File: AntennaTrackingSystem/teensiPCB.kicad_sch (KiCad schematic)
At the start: 0 parts

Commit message: 1st schematic built and added footprints
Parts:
- added C1: 0.1uF, Capacitor_SMD:C_0603_1608Metric, symbol Device:C
- added C2: 1uF, Capacitor_SMD:C_0603_1608Metric, symbol Device:C
- added J1: UART1, Connector_PinHeader_2.54mm:PinHeader_1x04_P2.54mm_Vertical, symbol Connector:Conn_01x04_Pin
- added J2: UART2, Connector_PinHeader_2.54mm:PinHeader_1x04_P2.54mm_Vertical, symbol Connector:Conn_01x04_Pin
- added J3: I2C ext, Connector_PinHeader_2.54mm:PinHeader_1x04_P2.54mm_Vertical, symbol Connector:Conn_01x04_Pin
- added J4: screw terminal, TerminalBlock_MetzConnect:TerminalBlock_MetzConnect_Type073_RT02602HBLU_1x02_P5.08mm_Horizontal, symbol Connector:Screw_Terminal_01x02
- added R1, R2: 4.7k, Resistor_SMD:R_0603_1608Metric, symbol Device:R
- added U1: Teensy4.1, Teensy41:Teensy41, symbol teensy:Teensy4.1
- added U2: SAM-M10Q-00B, SAM M10Q footprint:SAM-M10Q_UBL, symbol 2026-03-27_00-02-23:SAM-M10Q-00B
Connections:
- new net: J2.RX (Pin_2), U1.10 (8_TX2_IN1)
- new net: J2.TX (Pin_1), U1.9 (7_RX2_OUT1A)
- new net: J3.SCL (Pin_1), U1.16 (24_A10_TX6_SCL2)
- new net: J3.SDA (Pin_2), U1.17 (25_A11_RX6_SDA2)
- new net: J1.TX (Pin_1), U1.2 (0_RX1_CRX2_CS1)
- new net: J1.RX (Pin_2), U1.3 (1_TX1_CTX2_MISO1)
- new net: R2.1, U1.38 (16_A2_RX4_SCL1), U2.12 (SCL)
- new net: R1.2, U1.39 (17_A3_TX4_SDA1), U2.9 (SDA)
- new net: J4.2 (Pin_2), U1.48 (VIN)
- new net +3.3V: C1.1, C2.1, J1.3V3 (Pin_3), J2.3V3 (Pin_3), J3.3V3 (Pin_3), R1.1, R2.2, U1.15 (3V3), U1.46 (3V3), U2.17 (VCC)
- new net GND: C1.2, C2.2, J1.GND (Pin_4), J2.GND (Pin_4), J3.GND (Pin_4), J4.1 (Pin_1), U1.1 (GND), U1.47 (GND), U2.1 (GND), U2.10 (GND), U2.11 (GND), U2.15 (GND), U2.16 (GND), U2.20 (GND), U2.4 (GND), U2.5 (GND), U2.6 (GND)
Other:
- note added: "decoupling capacitors"
- note added: "pull up resistors"

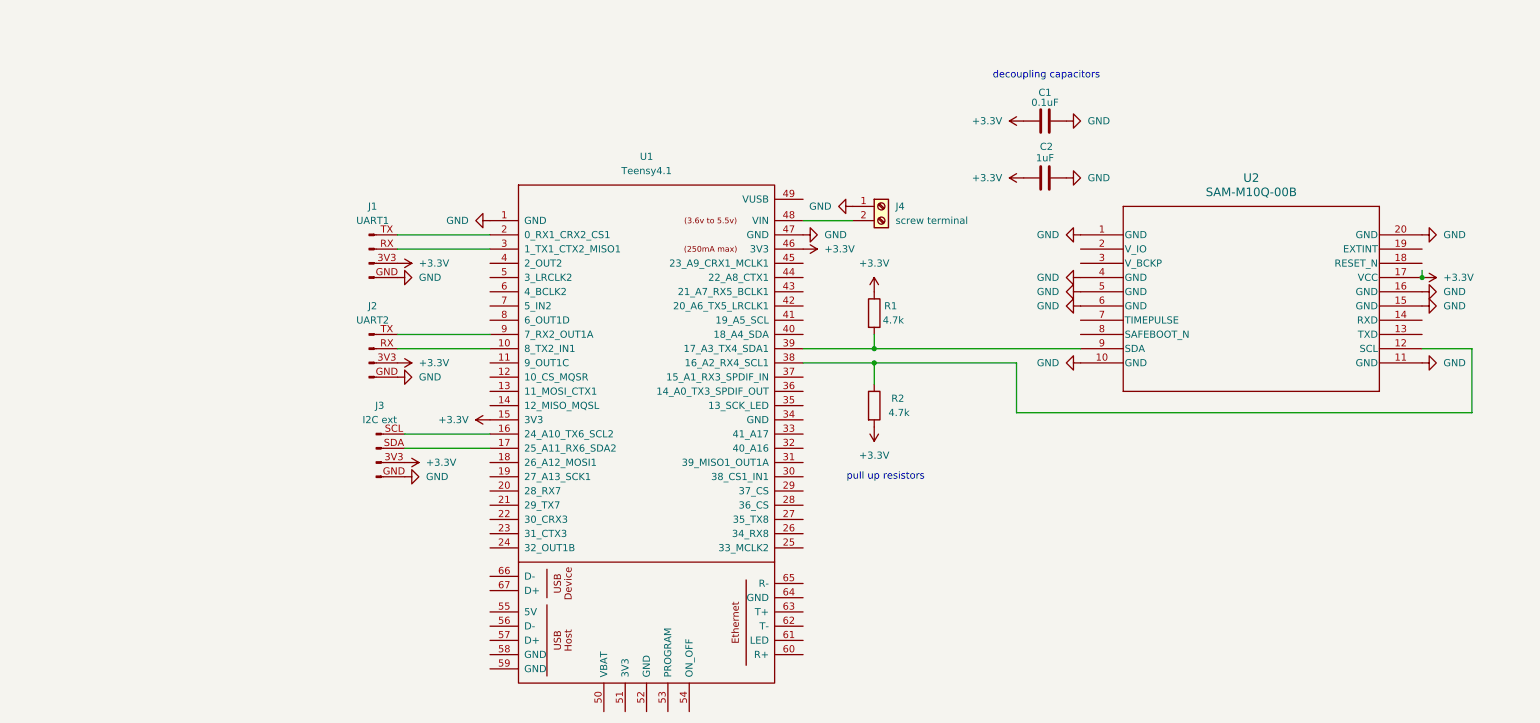
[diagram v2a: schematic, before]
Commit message: schematic review changes
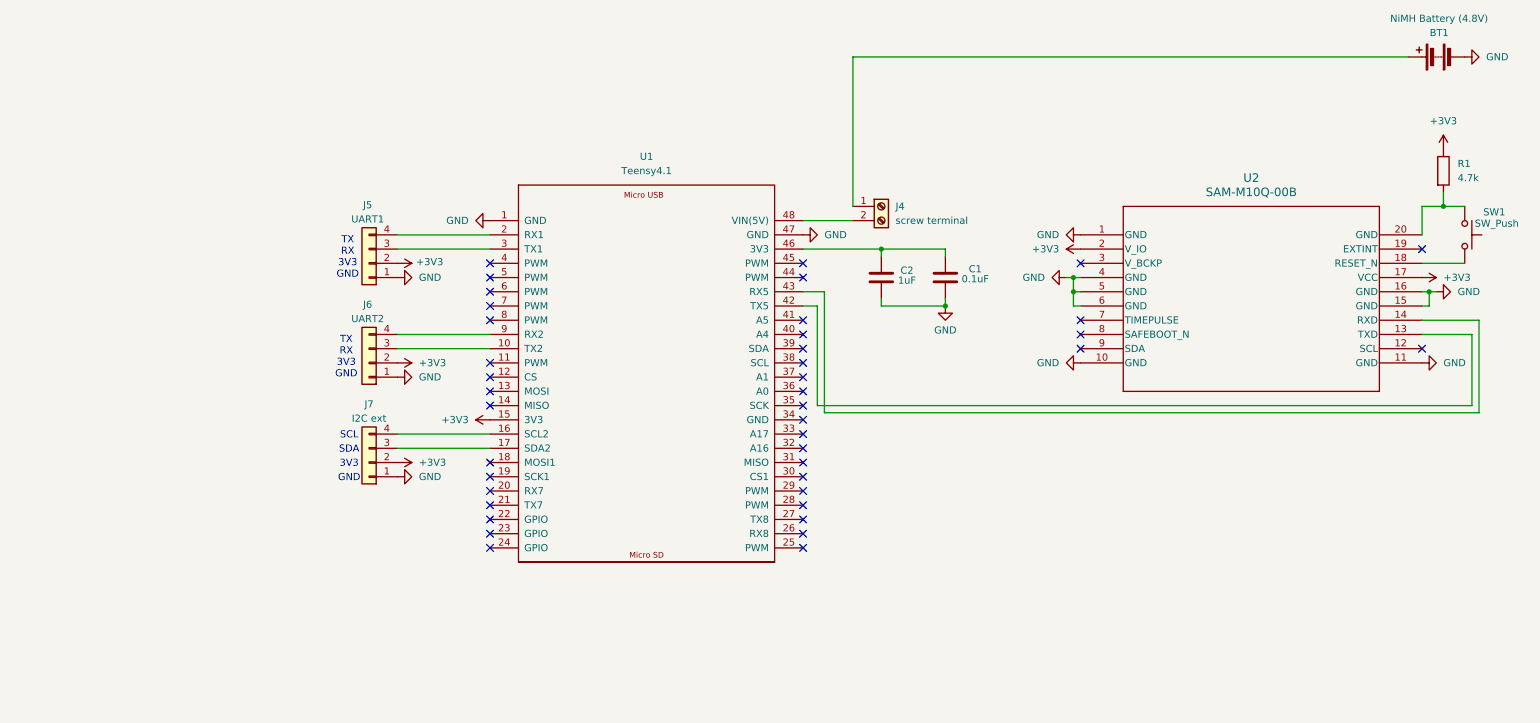
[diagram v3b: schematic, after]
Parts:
- removed J1: UART1, Connector_PinHeader_2.54mm:PinHeader_1x04_P2.54mm_Vertical, symbol Connector:Conn_01x04_Pin
- removed J2: UART2, Connector_PinHeader_2.54mm:PinHeader_1x04_P2.54mm_Vertical, symbol Connector:Conn_01x04_Pin
- removed J3: I2C ext, Connector_PinHeader_2.54mm:PinHeader_1x04_P2.54mm_Vertical, symbol Connector:Conn_01x04_Pin
- removed R2: 4.7k, Resistor_SMD:R_0603_1608Metric, symbol Device:R
- added BT1: NiMH Battery (4.8V), Battery:BatteryHolder_Keystone_2462_2xAA, symbol Device:Battery
- added J5: UART1, Connector_JST:JST_EH_B4B-EH-A_1x04_P2.50mm_Vertical, symbol Connector_Generic:Conn_01x04
- added J6: UART2, Connector_JST:JST_EH_B4B-EH-A_1x04_P2.50mm_Vertical, symbol Connector_Generic:Conn_01x04
- added J7: I2C ext, Connector_JST:JST_EH_B4B-EH-A_1x04_P2.50mm_Vertical, symbol Connector_Generic:Conn_01x04
- added SW1: SW_Push, Button_Switch_THT:SW_PUSH-12mm, symbol Switch:SW_Push
- U1: footprint Teensy41:Teensy41 -> Teensy41:TEENSY41
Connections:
- net GND: now also BT1.2 (-), J5.1 (Pin_1), J6.1 (Pin_1), J7.1 (Pin_1); no longer J4.1 (Pin_1), U2.20 (GND)
- net at U1.10 (TX2): now also J6.3 (Pin_3)
- net at U1.9 (RX2): now also J6.4 (Pin_4)
- net at U1.16 (SCL2): now also J7.4 (Pin_4)
- net at U1.17 (SDA2): now also J7.3 (Pin_3)
- net at U1.2 (RX1): now also J5.4 (Pin_4)
- net at U1.3 (TX1): now also J5.3 (Pin_3)
- net at U1.38 (SCL): no longer U2.12 (SCL)
- net at U1.42 (TX5): now also U2.13 (TXD)
- net at U1.43 (RX5): now also U2.14 (RXD)
- net at U2.18 (RESET_N): now also SW1.2
- net +3V3: now reaches U2.2 (V_IO)
- net +3V3: now also R1.1, U1.15 (3V3), U2.17 (VCC), J5.2 (Pin_2), J6.2 (Pin_2), J7.2 (Pin_2)
- net +3.3V: no longer names the net of C1.1, C2.1, U1.46 (3V3)
- net +3.3V: no longer R1.1, U1.15 (3V3), U2.17 (VCC)
- new net: R1.2, SW1.1, U2.20 (GND)
- new net: BT1.1 (+), J4.1 (Pin_1)
- now unconnected: U1.39 (17_A3_TX4_SDA1), U2.9 (SDA)
- no-connect marks 0 -> 41
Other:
- note added: "3V3"
- note added: "GND"
- note added: "SCL"
- note added: "SDA"
- note added: "TX RX 3V3 GND"
- note removed: "decoupling capacitors"
- note removed: "pull up resistors"
- title: (none) -> ATS_Teensy_breakout
- moved on the sheet: C1, C2

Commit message: cleanup
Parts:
- J5, J6, J7: footprint Connector_JST:JST_EH_B4B-EH-A_1x04_P2.50mm_Vertical -> Connector_JST:JST_XH_B4B-XH-A_1x04_P2.50mm_Vertical
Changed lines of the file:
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@@
 			)
 		)
-		(property "Footprint" "Connector_JST:JST_EH_B4B-EH-A_1x04_P2.50mm_Vertical"
+		(property "Footprint" "Connector_JST:JST_XH_B4B-XH-A_1x04_P2.50mm_Vertical"
 			(at 78.74 96.52 0)
 			(effects
@@
 			)
 		)
-		(property "Footprint" "Connector_JST:JST_EH_B4B-EH-A_1x04_P2.50mm_Vertical"
+		(property "Footprint" "Connector_JST:JST_XH_B4B-XH-A_1x04_P2.50mm_Vertical"
 			(at 78.74 78.74 0)
 			(effects
@@
 			)
 		)
-		(property "Footprint" "Connector_JST:JST_EH_B4B-EH-A_1x04_P2.50mm_Vertical"
+		(property "Footprint" "Connector_JST:JST_XH_B4B-XH-A_1x04_P2.50mm_Vertical"
 			(at 78.74 60.96 0)
 			(effects

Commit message: back to I2C and other small updates
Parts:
- removed BT1: NiMH Battery (4.8V), Battery:BatteryHolder_Keystone_2462_2xAA, symbol Device:Battery
- removed J4: screw terminal, TerminalBlock_MetzConnect:TerminalBlock_MetzConnect_Type073_RT02602HBLU_1x02_P5.08mm_Horizontal, symbol Connector:Screw_Terminal_01x02
- added J1: screw terminal, Connector_JST:JST_XH_B2B-XH-A_1x02_P2.50mm_Vertical, symbol Connector_Generic:Conn_01x02
- added R2, R3: 4.7k, Resistor_SMD:R_0603_1608Metric, symbol Device:R
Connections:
- net +3V3: now also J5.4 (Pin_4), J6.4 (Pin_4), J7.4 (Pin_4), R2.2, R3.1; no longer J5.2 (Pin_2), J6.2 (Pin_2), J7.2 (Pin_2)
- net GND: now also SW1.1, U2.20 (GND); no longer U1.47 (GND)
- net at U1.16 (SCL2): now also J7.2 (Pin_2); no longer J7.4 (Pin_4)
- net at U1.9 (RX2): now also J6.2 (Pin_2); no longer J6.4 (Pin_4)
- net at U1.2 (RX1): now also J5.2 (Pin_2); no longer J5.4 (Pin_4)
- net at U1.38 (SCL): now also U2.12 (SCL), R2.1
- net at U1.39 (SDA): now also U2.9 (SDA), R3.2
- net at U1.42 (TX5): no longer U2.13 (TXD)
- net at U1.43 (RX5): no longer U2.14 (RXD)
- net +V: now reaches U1.48 (VIN(5V))
- net +V: now also J1.1 (Pin_1)
- net at SW1.2, U2.18 (RESET_N): now also R1.2
- new net: J1.2 (Pin_2), U1.47 (GND)
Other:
- note added: "3V3 SDA SCL GND"
- note added: "3V3 TX RX GND"
- note removed: "3V3"
- note removed: "GND"
- note removed: "SCL"
- note removed: "SDA"
- note removed: "TX RX 3V3 GND"
- moved on the sheet: C1, C2, J5, J6, J7, R1, SW1, U1, U2

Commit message: final changes
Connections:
- net +3V3: now also U2.3 (V_BCKP)
- no-connect marks 41 -> 40
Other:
- note added: "I2C Address: 0x42"
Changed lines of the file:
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@@
+		)
+	)
+	(text "I2C Address: 0x42"
+		(exclude_from_sim no)
+		(at 135.382 77.724 0)
+		(effects
+			(font
+				(size 1.27 1.27)
+			)
 		)
 	)
@@
 	)
 	(no_connect
-		(at 161.29 60.96)
-	)
-	(no_connect
 		(at 55.88 81.28)
 	)
@@
 	(wire
 		(pts
-			(xy 49.53 73.66) (xy 49.53 76.2)
+			(xy 53.34 73.66) (xy 53.34 76.2)
 		)
 		(stroke
@@
 	(wire
 		(pts
-			(xy 49.53 76.2) (xy 55.88 76.2)
+			(xy 53.34 76.2) (xy 55.88 76.2)
 		)
 		(stroke
@@
 	(wire
 		(pts
-			(xy 26.67 73.66) (xy 49.53 73.66)
+			(xy 26.67 73.66) (xy 53.34 73.66)
 		)
 		(stroke
@@
 					(unit 1)
 				)
+			)
+		)
+	)
+	(symbol
+		(lib_id "power:+3V3")
+		(at 161.29 60.96 90)
+		(unit 1)
+		(exclude_from_sim no)
+		(in_bom yes)
+		(on_board yes)
+		(dnp no)
+		(fields_autoplaced yes)
+		(property "Reference" "#PWR021"
+			(at 165.1 60.96 0)
+			(effects
+				(font
+					(size 1.27 1.27)
+				)
+				(hide yes)
+			)
+		)
+		(property "Value" "+3V3"
+			(at 157.48 60.9599 90)
+			(effects
+				(font
+					(size 1.27 1.27)
+				)
+				(justify left)
+			)
+		)
+		(property "Footprint" ""
+			(at 161.29 60.96 0)
+			(effects
+				(font
+					(size 1.27 1.27)
+				)
+				(hide yes)
+			)
+		)
+		(property "Datasheet" ""
+			(at 161.29 60.96 0)
+			(effects
+				(font
+					(size 1.27 1.27)
+				)
+				(hide yes)
+			)
+		)
+		(property "Description" "Power symbol creates a global label with name \"+3V3\""
+			(at 161.29 60.96 0)
+			(effects
+				(font
+					(size 1.27 1.27)
+				)
+				(hide yes)
+			)
+		)
+		(pin "1"
+		)
+		(instances
+			(project "teensiPCB"
+				(path "/ba786cef-8ef6-45a2-be74-19524883f146"
+					(reference "#PWR021")
+					(unit 1)
+				)

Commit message: changes
added battery chnages
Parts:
- added J2: Conn_01x02, Connector_JST:JST_XH_B2B-XH-A_1x02_P2.50mm_Vertical, symbol Connector_Generic:Conn_01x02
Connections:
- net +V: now also J2.1 (Pin_1); no longer J1.1 (Pin_1)
- net GND: now also J1.2 (Pin_2), U1.47 (GND)
- new net: J1.1 (Pin_1), J2.2 (Pin_2)
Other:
- moved on the sheet: J1
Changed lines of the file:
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@@
 		(color 0 0 0 0)
 	)
+	(junction
+		(at 132.08 46.99)
+		(diameter 0)
+		(color 0 0 0 0)
+	)
 	(no_connect
 		(at 111.76 81.28)
@@
 	(wire
 		(pts
+			(xy 119.38 55.88) (xy 111.76 55.88)
+		)
+		(stroke
+			(width 0)
+			(type default)
+		)
+	)
+	(wire
+		(pts
 			(xy 53.34 73.66) (xy 53.34 76.2)
 		)
@@
 	(wire
 		(pts
+			(xy 118.11 44.45) (xy 118.11 53.34)
+		)
+		(stroke
+			(width 0)
+			(type default)
+		)
+	)
+	(wire
+		(pts
 			(xy 160.02 63.5) (xy 161.29 63.5)
 		)
@@
 	(wire
 		(pts
-			(xy 111.76 53.34) (xy 120.65 53.34)
-		)
-		(stroke
-			(width 0)
-			(type default)
-		)
-	)
-	(wire
-		(pts
 			(xy 52.07 58.42) (xy 55.88 58.42)
 		)
@@
 	(wire
 		(pts
+			(xy 118.11 44.45) (xy 124.46 44.45)
+		)
+		(stroke
+			(width 0)
+			(type default)
+		)
+	)
+	(wire
+		(pts
 			(xy 26.67 58.42) (xy 40.64 58.42)
 		)
@@
 	(wire
 		(pts
+			(xy 119.38 46.99) (xy 119.38 55.88)
+		)
+		(stroke
+			(width 0)
+			(type default)
+		)
+	)
+	(wire
+		(pts
 			(xy 222.25 50.8) (xy 222.25 55.88)
 		)
@@
 	(wire
 		(pts
+			(xy 127 44.45) (xy 140.97 44.45)
+		)
+		(stroke
+			(width 0)
+			(type default)
+		)
+	)
+	(wire
+		(pts
 			(xy 151.13 78.74) (xy 151.13 85.09)
 		)
@@
 	(wire
 		(pts
-			(xy 111.76 55.88) (xy 120.65 55.88)
+			(xy 119.38 46.99) (xy 132.08 46.99)
 		)
 		(stroke
@@
 		(pts
 			(xy 26.67 73.66) (xy 53.34 73.66)
+		)
+		(stroke
+			(width 0)
+			(type default)
+		)
+	)
+	(wire
+		(pts
+			(xy 132.08 46.99) (xy 140.97 46.99)
+		)
+		(stroke
+			(width 0)
+			(type default)
+		)
+	)
+	(wire
+		(pts
+			(xy 118.11 53.34) (xy 111.76 53.34)
 		)
 		(stroke
@@
 	)
 	(symbol
+		(lib_id "Connector_Generic:Conn_01x02")
+		(at 124.46 39.37 90)
+		(unit 1)
+		(exclude_from_sim no)
+		(in_bom yes)
+		(on_board yes)
+		(dnp no)
+		(fields_autoplaced yes)
+		(property "Reference" "J2"
+			(at 129.54 38.0999 90)
+			(effects
+				(font
+					(size 1.27 1.27)
+				)
+				(justify right)
+			)
+		)
+		(property "Value" "Conn_01x02"
+			(at 129.54 40.6399 90)
+			(effects
+				(font
+					(size 1.27 1.27)
+				)
+				(justify right)
+			)
+		)
+		(property "Footprint" "Connector_JST:JST_XH_B2B-XH-A_1x02_P2.50mm_Vertical"
+			(at 124.46 39.37 0)
+			(effects
+				(font
+					(size 1.27 1.27)
+				)
+				(hide yes)
+			)
+		)
+		(property "Datasheet" "~"
+			(at 124.46 39.37 0)
+			(effects
+				(font
+					(size 1.27 1.27)
+				)
+				(hide yes)
+			)
+		)
+		(property "Description" "Generic connector, single row, 01x02, script generated (kicad-library-utils/schlib/autogen/connector/)"
+			(at 124.46 39.37 0)
+			(effects
+				(font
+					(size 1.27 1.27)
+				)
+				(hide yes)
+			)
+		)
+		(pin "2"
+		)
+		(pin "1"
+		)
+		(instances
+			(project ""
+				(path "/ba786cef-8ef6-45a2-be74-19524883f146"
+					(reference "J2")
+					(unit 1)
+				)
+			)
+		)
+	)
+	(symbol
 		(lib_id "power:+3V3")
 		(at 26.67 53.34 270)
@@
 	)
 	(symbol
+		(lib_id "power:GND")
+		(at 132.08 46.99 0)
+		(unit 1)
+		(exclude_from_sim no)
+		(in_bom yes)
+		(on_board yes)
+		(dnp no)
+		(fields_autoplaced yes)
+		(property "Reference" "#PWR022"
+			(at 132.08 53.34 0)
+			(effects
+				(font
+					(size 1.27 1.27)
+				)
+				(hide yes)
+			)
+		)
+		(property "Value" "GND"
+			(at 132.08 52.07 0)
+			(effects
+				(font
+					(size 1.27 1.27)
+				)
+			)
+		)
+		(property "Footprint" ""
+			(at 132.08 46.99 0)
+			(effects
+				(font
+					(size 1.27 1.27)
+				)
+				(hide yes)
+			)
+		)
+		(property "Datasheet" ""
+			(at 132.08 46.99 0)
+			(effects
+				(font
+					(size 1.27 1.27)
+				)
+				(hide yes)
+			)
+		)
+		(property "Description" "Power symbol creates a global label with name \"GND\" , ground"
+			(at 132.08 46.99 0)
+			(effects
+				(font
+					(size 1.27 1.27)
+				)
+				(hide yes)
+			)
+		)
+		(pin "1"
+		)
+		(instances
+			(project ""
+				(path "/ba786cef-8ef6-45a2-be74-19524883f146"
+					(reference "#PWR022")
+					(unit 1)
+				)
+			)
+		)
+	)
+	(symbol
 		(lib_id "Device:R")
 		(at 144.78 72.39 0)
@@
 	(symbol
 		(lib_id "Connector_Generic:Conn_01x02")
-		(at 125.73 53.34 0)
+		(at 146.05 44.45 0)
 		(unit 1)
 		(exclude_from_sim no)
@@
 		(fields_autoplaced yes)
 		(property "Reference" "J1"
-			(at 128.27 53.3399 0)
+			(at 148.59 44.4499 0)
 			(effects
 				(font
@@
 		)
 		(property "Value" "screw terminal"
-			(at 128.27 55.8799 0)
+			(at 148.59 46.9899 0)
 			(effects
 				(font
@@
 		)
 		(property "Footprint" "Connector_JST:JST_XH_B2B-XH-A_1x02_P2.50mm_Vertical"
-			(at 125.73 53.34 0)
+			(at 146.05 44.45 0)
 			(effects
 				(font
@@
 		)
 		(property "Datasheet" "~"
-			(at 125.73 53.34 0)
+			(at 146.05 44.45 0)
 			(effects
 				(font
@@
 		)
 		(property "Description" "Generic connector, single row, 01x02, script generated (kicad-library-utils/schlib/autogen/connector/)"
-			(at 125.73 53.34 0)
-			(effects
-				(font
+			(at 146.05 44.45 0)
+			(effects
+				(font
